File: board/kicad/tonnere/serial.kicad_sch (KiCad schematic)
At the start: 1 part, among them J12 STM USART TTL

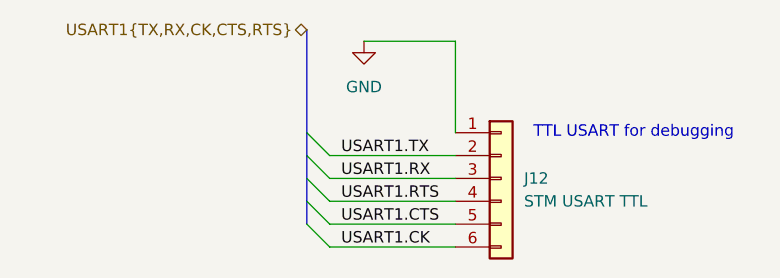
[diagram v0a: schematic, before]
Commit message: 0.60 (not final). Fix errata from 0.51. Added USB2 phy.
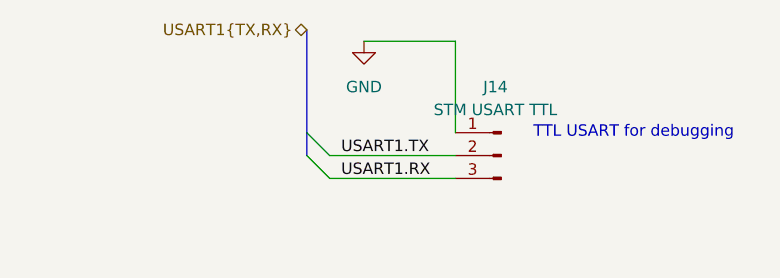
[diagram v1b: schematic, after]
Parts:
- removed J12: STM USART TTL, Connector_PinHeader_2.54mm:PinHeader_1x06_P2.54mm_Vertical, symbol Connector_Generic:Conn_01x06
- added J14: STM USART TTL, Connector_PinSocket_2.54mm:PinSocket_1x03_P2.54mm_Vertical, symbol Connector:Conn_01x03_Pin
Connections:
- net GND: now also J14.1 (Pin_1)
- net USART1.RX: now also J14.3 (Pin_3)
- net USART1.TX: now also J14.2 (Pin_2)
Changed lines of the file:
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@@
-	)
-	(bus_entry
-		(at 52.07 45.72)
-		(size 2.54 2.54)
-		(stroke
-			(width 0)
-			(type default)
-		)
-	)
-	(bus_entry
-		(at 52.07 48.26)
-		(size 2.54 2.54)
-		(stroke
-			(width 0)
-			(type default)
-		)
-	)
-	(bus_entry
-		(at 52.07 43.18)
-		(size 2.54 2.54)
-		(stroke
-			(width 0)
-			(type default)
-		)
 	)
 	(bus_entry
@@
 	(bus
 		(pts
-			(xy 52.07 40.64) (xy 52.07 43.18)
+			(xy 52.07 38.1) (xy 52.07 40.64)
+		)
+		(stroke
+			(width 0)
+			(type default)
+		)
+	)
+	(wire
+		(pts
+			(xy 54.61 43.18) (xy 68.58 43.18)
+		)
+		(stroke
+			(width 0)
+			(type default)
+		)
+	)
+	(wire
+		(pts
+			(xy 54.61 40.64) (xy 68.58 40.64)
+		)
+		(stroke
+			(width 0)
+			(type default)
+		)
+	)
+	(wire
+		(pts
+			(xy 68.58 27.94) (xy 68.58 38.1)
 		)
 		(stroke
@@
 	(bus
 		(pts
-			(xy 52.07 38.1) (xy 52.07 40.64)
-		)
-		(stroke
-			(width 0)
-			(type default)
-		)
-	)
-	(wire
-		(pts
-			(xy 54.61 43.18) (xy 68.58 43.18)
-		)
-		(stroke
-			(width 0)
-			(type default)
-		)
-	)
-	(wire
-		(pts
-			(xy 54.61 40.64) (xy 68.58 40.64)
-		)
-		(stroke
-			(width 0)
-			(type default)
-		)
-	)
-	(wire
-		(pts
-			(xy 68.58 27.94) (xy 68.58 38.1)
-		)
-		(stroke
-			(width 0)
-			(type default)
-		)
-	)
-	(wire
-		(pts
-			(xy 54.61 48.26) (xy 68.58 48.26)
-		)
-		(stroke
-			(width 0)
-			(type default)
-		)
-	)
-	(bus
-		(pts
-			(xy 52.07 45.72) (xy 52.07 48.26)
-		)
-		(stroke
-			(width 0)
-			(type default)
-		)
-	)
-	(bus
-		(pts
 			(xy 52.07 26.67) (xy 52.07 38.1)
 		)
@@
 		)
 	)
-	(bus
-		(pts
-			(xy 52.07 43.18) (xy 52.07 45.72)
-		)
-		(stroke
-			(width 0)
-			(type default)
-		)
-	)
-	(wire
-		(pts
-			(xy 54.61 45.72) (xy 68.58 45.72)
-		)
-		(stroke
-			(width 0)
-			(type default)
-		)
-	)
 	(wire
 		(pts
 			(xy 58.42 27.94) (xy 68.58 27.94)
-		)
-		(stroke
-			(width 0)
-			(type default)
-		)
-	)
-	(wire
-		(pts
-			(xy 54.61 50.8) (xy 68.58 50.8)
 		)
 		(stroke
@@
 		)
 	)
-	(label "USART1.RTS"
-		(at 55.88 45.72 0)
-		(effects
-			(font
-				(size 1.27 1.27)
-			)
-			(justify left bottom)
-		)
-	)
-	(label "USART1.CK"
-		(at 55.88 50.8 0)
-		(effects
-			(font
-				(size 1.27 1.27)
-			)
-			(justify left bottom)
-		)
-	)
-	(label "USART1.CTS"
-		(at 55.88 48.26 0)
-		(effects
-			(font
-				(size 1.27 1.27)
-			)
-			(justify left bottom)
-		)
-	)
-	(hierarchical_label "USART1{TX,RX,CK,CTS,RTS}"
+	(hierarchical_label "USART1{TX,RX}"
 		(shape bidirectional)
 		(at 52.07 26.67 180)
@@
 	)
 	(symbol
-		(lib_id "Connector_Generic:Conn_01x06")
-		(at 73.66 43.18 0)
+		(lib_id "Connector:Conn_01x03_Pin")
+		(at 73.66 40.64 0)
+		(mirror y)
 		(unit 1)
 		(exclude_from_sim no)
@@
 		(on_board yes)
 		(dnp no)
-		(fields_autoplaced yes)
-		(property "Reference" "J12"
-			(at 76.2 43.1799 0)
-			(effects
-				(font
-					(size 1.27 1.27)
-				)
-				(justify left)
+		(property "Reference" "J14"
+			(at 73.025 33.02 0)
+			(effects
+				(font
+					(size 1.27 1.27)
+				)
 			)
 		)
 		(property "Value" "STM USART TTL"
-			(at 76.2 45.7199 0)
-			(effects
-				(font
-					(size 1.27 1.27)
-				)
-				(justify left)
-			)
-		)
-		(property "Footprint" "Connector_PinHeader_2.54mm:PinHeader_1x06_P2.54mm_Vertical"
-			(at 73.66 43.18 0)
+			(at 73.025 35.56 0)
+			(effects
+				(font
+					(size 1.27 1.27)
+				)
+			)
+		)
+		(property "Footprint" "Connector_PinSocket_2.54mm:PinSocket_1x03_P2.54mm_Vertical"
+			(at 73.66 40.64 0)
 			(effects
 				(font
@@
 		)
 		(property "Datasheet" "~"
-			(at 73.66 43.18 0)
-			(effects
-				(font
-					(size 1.27 1.27)
-				)
-				(hide yes)
-			)
-		)
-		(property "Description" "Generic connector, single row, 01x06, script generated (kicad-library-utils/schlib/autogen/connector/)"
-			(at 73.66 43.18 0)
+			(at 73.66 40.64 0)
+			(effects
+				(font
+					(size 1.27 1.27)
+				)
+				(hide yes)
+			)
+		)
+		(property "Description" "Generic connector, single row, 01x03, script generated"
+			(at 73.66 40.64 0)
 			(effects
 				(font
@@
 		(pin "3"
 		)
-		(pin "5"
-		)
 		(pin "1"
 		)
-		(pin "4"
-		)
 		(pin "2"
-		)
-		(pin "6"
 		)
 		(instances
 			(project ""
 				(path "/eb8e239c-f2ec-4b57-8f5c-6c75d6b59ab3/ffed6702-cf67-401e-a39f-b369f1396c7d"
-					(reference "J12")
+					(reference "J14")
 					(unit 1)
 				)
